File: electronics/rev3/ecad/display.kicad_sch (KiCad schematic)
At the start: 61 parts, among them Q1 2N7002, Q10 BSS84, Q11 BSS84, Q12 2N7002, Q13 BSS84, Q15 2N7002, Q16 2N7002, Q17 2N7002, Q18 2N7002, Q19 2N7002, Q2 2N7002, Q20 2N7002, Q21 2N7002, Q22 2N7002, Q23 2N7002, Q24 2N7002, Q3 2N7002, Q4 2N7002, Q5 BSS84, Q6 BSS84, Q7 BSS84, Q8 BSS84, Q9 BSS84, U4 CC56-12SURKWA

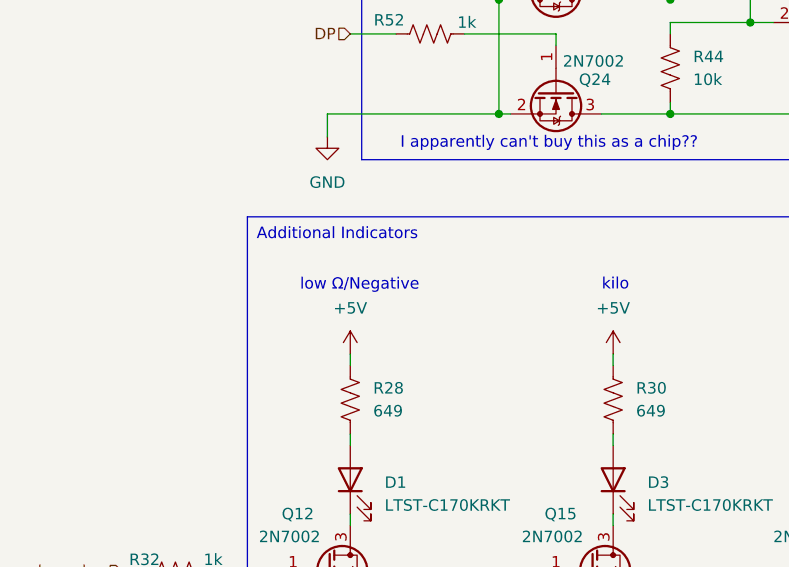
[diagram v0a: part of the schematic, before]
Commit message: rev3 schematic work
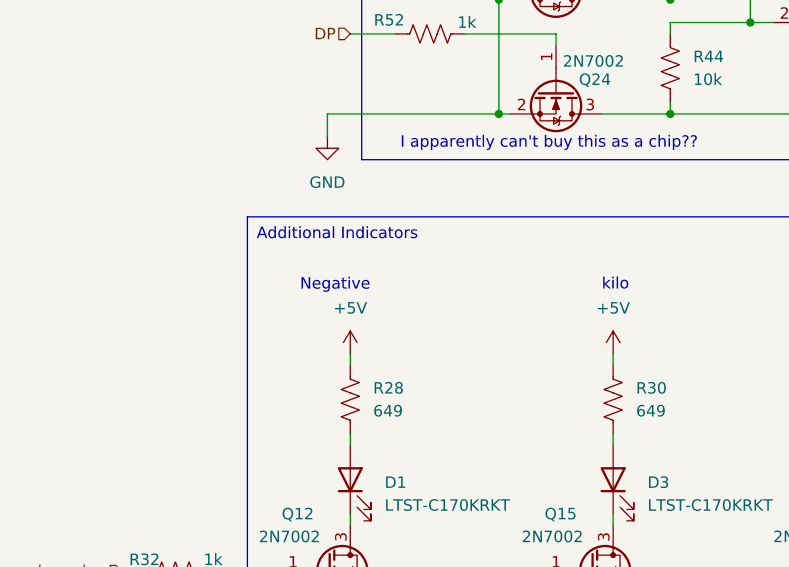
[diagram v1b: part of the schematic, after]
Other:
- note added: "Negative"
- note removed: "low Ω/Negative"
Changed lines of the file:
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@@
 		)
 	)
-	(text "low Ω/Negative"
+	(text "Negative"
 		(exclude_from_sim no)
 		(at 50.292 144.272 0)

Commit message: layout work rev3
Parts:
- R10, R11, R12, R13, R14, R15, R16, R17, R18, R19, R20, R23, R24, R25, R26, R27, R28, R30, R31, R32, R34, R35, R43, R44, R45, R46, R47, R48, R49, R50, R51, R52, R6, R9: footprint Resistor_SMD:R_0805_2012Metric_Pad1.20x1.40mm_HandSolder -> Resistor_SMD:R_0805_2012Metric
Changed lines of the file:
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@@
 			)
 		)
-		(property "Footprint" "Resistor_SMD:R_0805_2012Metric_Pad1.20x1.40mm_HandSolder"
+		(property "Footprint" "Resistor_SMD:R_0805_2012Metric"
 			(at 131.064 34.544 90)
 			(effects
@@
 			)
 		)
-		(property "Footprint" "Resistor_SMD:R_0805_2012Metric_Pad1.20x1.40mm_HandSolder"
+		(property "Footprint" "Resistor_SMD:R_0805_2012Metric"
 			(at 155.194 81.534 90)
 			(effects
@@
 			)
 		)
-		(property "Footprint" "Resistor_SMD:R_0805_2012Metric_Pad1.20x1.40mm_HandSolder"
+		(property "Footprint" "Resistor_SMD:R_0805_2012Metric"
 			(at 92.456 119.634 90)
 			(effects
@@
 			)
 		)
-		(property "Footprint" "Resistor_SMD:R_0805_2012Metric_Pad1.20x1.40mm_HandSolder"
+		(property "Footprint" "Resistor_SMD:R_0805_2012Metric"
 			(at 37.084 192.024 90)
 			(effects
@@
 			)
 		)
-		(property "Footprint" "Resistor_SMD:R_0805_2012Metric_Pad1.20x1.40mm_HandSolder"
+		(property "Footprint" "Resistor_SMD:R_0805_2012Metric"
 			(at 155.194 100.584 90)
 			(effects
@@
 			)
 		)
-		(property "Footprint" "Resistor_SMD:R_0805_2012Metric_Pad1.20x1.40mm_HandSolder"
+		(property "Footprint" "Resistor_SMD:R_0805_2012Metric"
 			(at 92.456 56.134 90)
 			(effects
@@
 			)
 		)
-		(property "Footprint" "Resistor_SMD:R_0805_2012Metric_Pad1.20x1.40mm_HandSolder"
+		(property "Footprint" "Resistor_SMD:R_0805_2012Metric"
 			(at 92.456 81.534 90)
 			(effects
@@
 			)
 		)
-		(property "Footprint" "Resistor_SMD:R_0805_2012Metric_Pad1.20x1.40mm_HandSolder"
+		(property "Footprint" "Resistor_SMD:R_0805_2012Metric"
 			(at 65.024 114.554 90)
 			(effects
@@
 			)
 		)
-		(property "Footprint" "Resistor_SMD:R_0805_2012Metric_Pad1.20x1.40mm_HandSolder"
+		(property "Footprint" "Resistor_SMD:R_0805_2012Metric"
 			(at 65.024 25.654 90)
 			(effects
@@
 			)
 		)
-		(property "Footprint" "Resistor_SMD:R_0805_2012Metric_Pad1.20x1.40mm_HandSolder"
+		(property "Footprint" "Resistor_SMD:R_0805_2012Metric"
 			(at 92.456 94.234 90)
 			(effects
@@
 			)
 		)
-		(property "Footprint" "Resistor_SMD:R_0805_2012Metric_Pad1.20x1.40mm_HandSolder"
+		(property "Footprint" "Resistor_SMD:R_0805_2012Metric"
 			(at 92.456 43.434 90)
 			(effects
@@
 			)
 		)
-		(property "Footprint" "Resistor_SMD:R_0805_2012Metric_Pad1.20x1.40mm_HandSolder"
+		(property "Footprint" "Resistor_SMD:R_0805_2012Metric"
 			(at 86.106 156.464 90)
 			(effects
@@
 			)
 		)
-		(property "Footprint" "Resistor_SMD:R_0805_2012Metric_Pad1.20x1.40mm_HandSolder"
+		(property "Footprint" "Resistor_SMD:R_0805_2012Metric"
 			(at 37.084 174.244 90)
 			(effects
@@
 			)
 		)
-		(property "Footprint" "Resistor_SMD:R_0805_2012Metric_Pad1.20x1.40mm_HandSolder"
+		(property "Footprint" "Resistor_SMD:R_0805_2012Metric"
 			(at 131.064 37.084 90)
 			(effects
@@
 			)
 		)
-		(property "Footprint" "Resistor_SMD:R_0805_2012Metric_Pad1.20x1.40mm_HandSolder"
+		(property "Footprint" "Resistor_SMD:R_0805_2012Metric"
 			(at 65.024 89.154 90)
 			(effects
@@
 			)
 		)
-		(property "Footprint" "Resistor_SMD:R_0805_2012Metric_Pad1.20x1.40mm_HandSolder"
+		(property "Footprint" "Resistor_SMD:R_0805_2012Metric"
 			(at 92.456 68.834 90)
 			(effects
@@
 			)
 		)
-		(property "Footprint" "Resistor_SMD:R_0805_2012Metric_Pad1.20x1.40mm_HandSolder"
+		(property "Footprint" "Resistor_SMD:R_0805_2012Metric"
 			(at 131.064 42.164 90)
 			(effects
@@
 			)
 		)
-		(property "Footprint" "Resistor_SMD:R_0805_2012Metric_Pad1.20x1.40mm_HandSolder"
+		(property "Footprint" "Resistor_SMD:R_0805_2012Metric"
 			(at 65.024 38.354 90)
 			(effects
@@
 			)
 		)
-		(property "Footprint" "Resistor_SMD:R_0805_2012Metric_Pad1.20x1.40mm_HandSolder"
+		(property "Footprint" "Resistor_SMD:R_0805_2012Metric"
 			(at 131.064 24.384 90)
 			(effects
@@
 			)
 		)
-		(property "Footprint" "Resistor_SMD:R_0805_2012Metric_Pad1.20x1.40mm_HandSolder"
+		(property "Footprint" "Resistor_SMD:R_0805_2012Metric"
 			(at 131.064 32.004 90)
 			(effects
@@
 			)
 		)
-		(property "Footprint" "Resistor_SMD:R_0805_2012Metric_Pad1.20x1.40mm_HandSolder"
+		(property "Footprint" "Resistor_SMD:R_0805_2012Metric"
 			(at 56.896 156.464 90)
 			(effects
@@
 			)
 		)
-		(property "Footprint" "Resistor_SMD:R_0805_2012Metric_Pad1.20x1.40mm_HandSolder"
+		(property "Footprint" "Resistor_SMD:R_0805_2012Metric"
 			(at 131.064 39.624 90)
 			(effects
@@
 			)
 		)
-		(property "Footprint" "Resistor_SMD:R_0805_2012Metric_Pad1.20x1.40mm_HandSolder"
+		(property "Footprint" "Resistor_SMD:R_0805_2012Metric"
 			(at 92.456 30.734 90)
 			(effects
@@
 			)
 		)
-		(property "Footprint" "Resistor_SMD:R_0805_2012Metric_Pad1.20x1.40mm_HandSolder"
+		(property "Footprint" "Resistor_SMD:R_0805_2012Metric"
 			(at 65.024 51.054 90)
 			(effects
@@
 			)
 		)
-		(property "Footprint" "Resistor_SMD:R_0805_2012Metric_Pad1.20x1.40mm_HandSolder"
+		(property "Footprint" "Resistor_SMD:R_0805_2012Metric"
 			(at 131.064 26.924 90)
 			(effects
@@
 			)
 		)
-		(property "Footprint" "Resistor_SMD:R_0805_2012Metric_Pad1.20x1.40mm_HandSolder"
+		(property "Footprint" "Resistor_SMD:R_0805_2012Metric"
 			(at 65.024 101.854 90)
 			(effects
@@
 			)
 		)
-		(property "Footprint" "Resistor_SMD:R_0805_2012Metric_Pad1.20x1.40mm_HandSolder"
+		(property "Footprint" "Resistor_SMD:R_0805_2012Metric"
 			(at 65.024 76.454 90)
 			(effects
@@
 			)
 		)
-		(property "Footprint" "Resistor_SMD:R_0805_2012Metric_Pad1.20x1.40mm_HandSolder"
+		(property "Footprint" "Resistor_SMD:R_0805_2012Metric"
 			(at 155.194 71.374 90)
 			(effects
@@
 			)
 		)
-		(property "Footprint" "Resistor_SMD:R_0805_2012Metric_Pad1.20x1.40mm_HandSolder"
+		(property "Footprint" "Resistor_SMD:R_0805_2012Metric"
 			(at 92.456 106.934 90)
 			(effects
@@
 			)
 		)
-		(property "Footprint" "Resistor_SMD:R_0805_2012Metric_Pad1.20x1.40mm_HandSolder"
+		(property "Footprint" "Resistor_SMD:R_0805_2012Metric"
 			(at 155.194 91.694 90)
 			(effects
@@
 			)
 		)
-		(property "Footprint" "Resistor_SMD:R_0805_2012Metric_Pad1.20x1.40mm_HandSolder"
+		(property "Footprint" "Resistor_SMD:R_0805_2012Metric"
 			(at 131.064 29.464 90)
 			(effects
@@
 			)
 		)
-		(property "Footprint" "Resistor_SMD:R_0805_2012Metric_Pad1.20x1.40mm_HandSolder"
+		(property "Footprint" "Resistor_SMD:R_0805_2012Metric"
 			(at 65.024 63.754 90)
 			(effects
@@
 			)
 		)
-		(property "Footprint" "Resistor_SMD:R_0805_2012Metric_Pad1.20x1.40mm_HandSolder"
+		(property "Footprint" "Resistor_SMD:R_0805_2012Metric"
 			(at 114.046 156.464 90)
 			(effects
@@
 			)
 		)
-		(property "Footprint" "Resistor_SMD:R_0805_2012Metric_Pad1.20x1.40mm_HandSolder"
+		(property "Footprint" "Resistor_SMD:R_0805_2012Metric"
 			(at 37.084 195.834 90)
 			(effects
